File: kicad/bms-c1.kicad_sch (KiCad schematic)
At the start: 33 parts, among them J1 MicroFit 2x12, J2 B4B-PH-SM4, J3 USB_B_Micro, J4 B3B-PH-SM4, J5 B2B-PH-SM4, J6 B4B-PH-SM4, P1 CONN_01X01, P2 CONN_01X01, P3 CONN_01X01, P4 CONN_01X01, P5 CONN_01X01

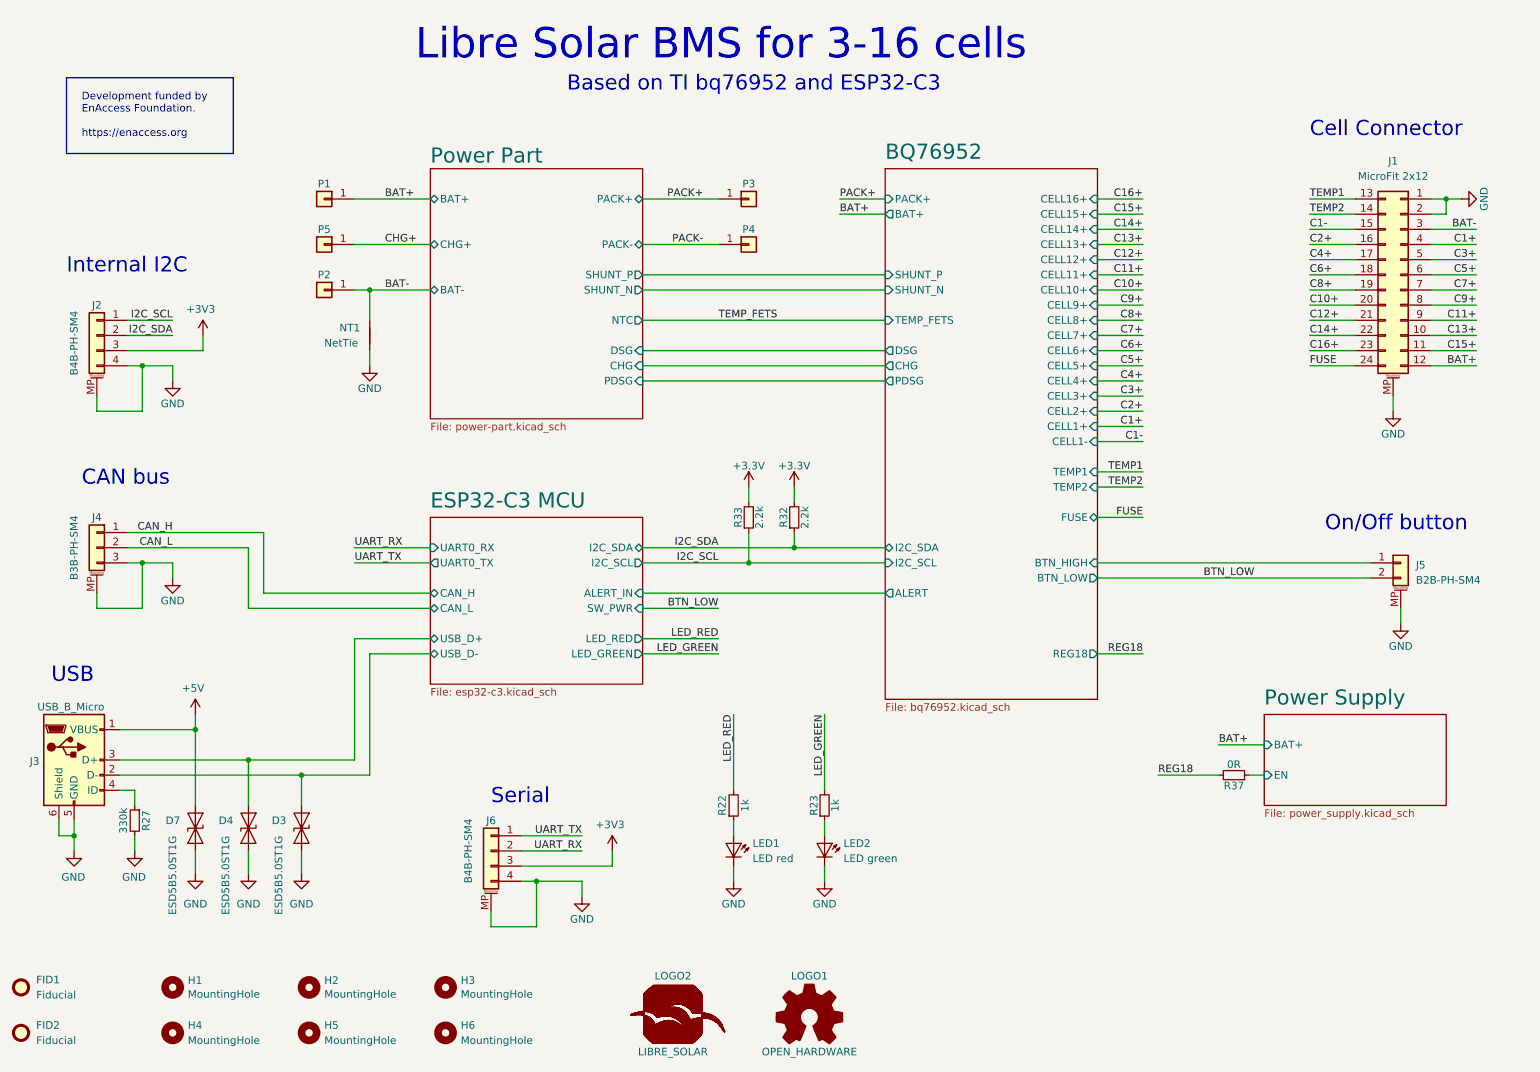
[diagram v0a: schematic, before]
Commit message: v0.4.0: Multiple improvements for new board revision
- Use LMR38010 for internal power supply (max. 80V instead of 60V)
- Change USB connector from Micro-A to C and remove 5V power supply
  which was not working anyway. The board cannot be powered by USB
  only.
- Add TS2 (connected to DFETOFF) to measure shunt temperature
- Add RS-485 transceiver (sharing the connector with CAN)
- Switch I2C pins of ESP32-C3 to GPIO8/9. This allows to re-use the
  I2C pull-ups for strapping configuration and frees two pins for the
  RS-485 transceiver RE and DE pins. Also we may get rid of the I2C
  glitches during start-up.
- Use 80V instead of 100V power MOSFETs to reduce Rds(on).
- Reduce DSG gate resistor R57 to 47R to increase switch-off speed.
- Adjust some resistors to reduce number of different parts
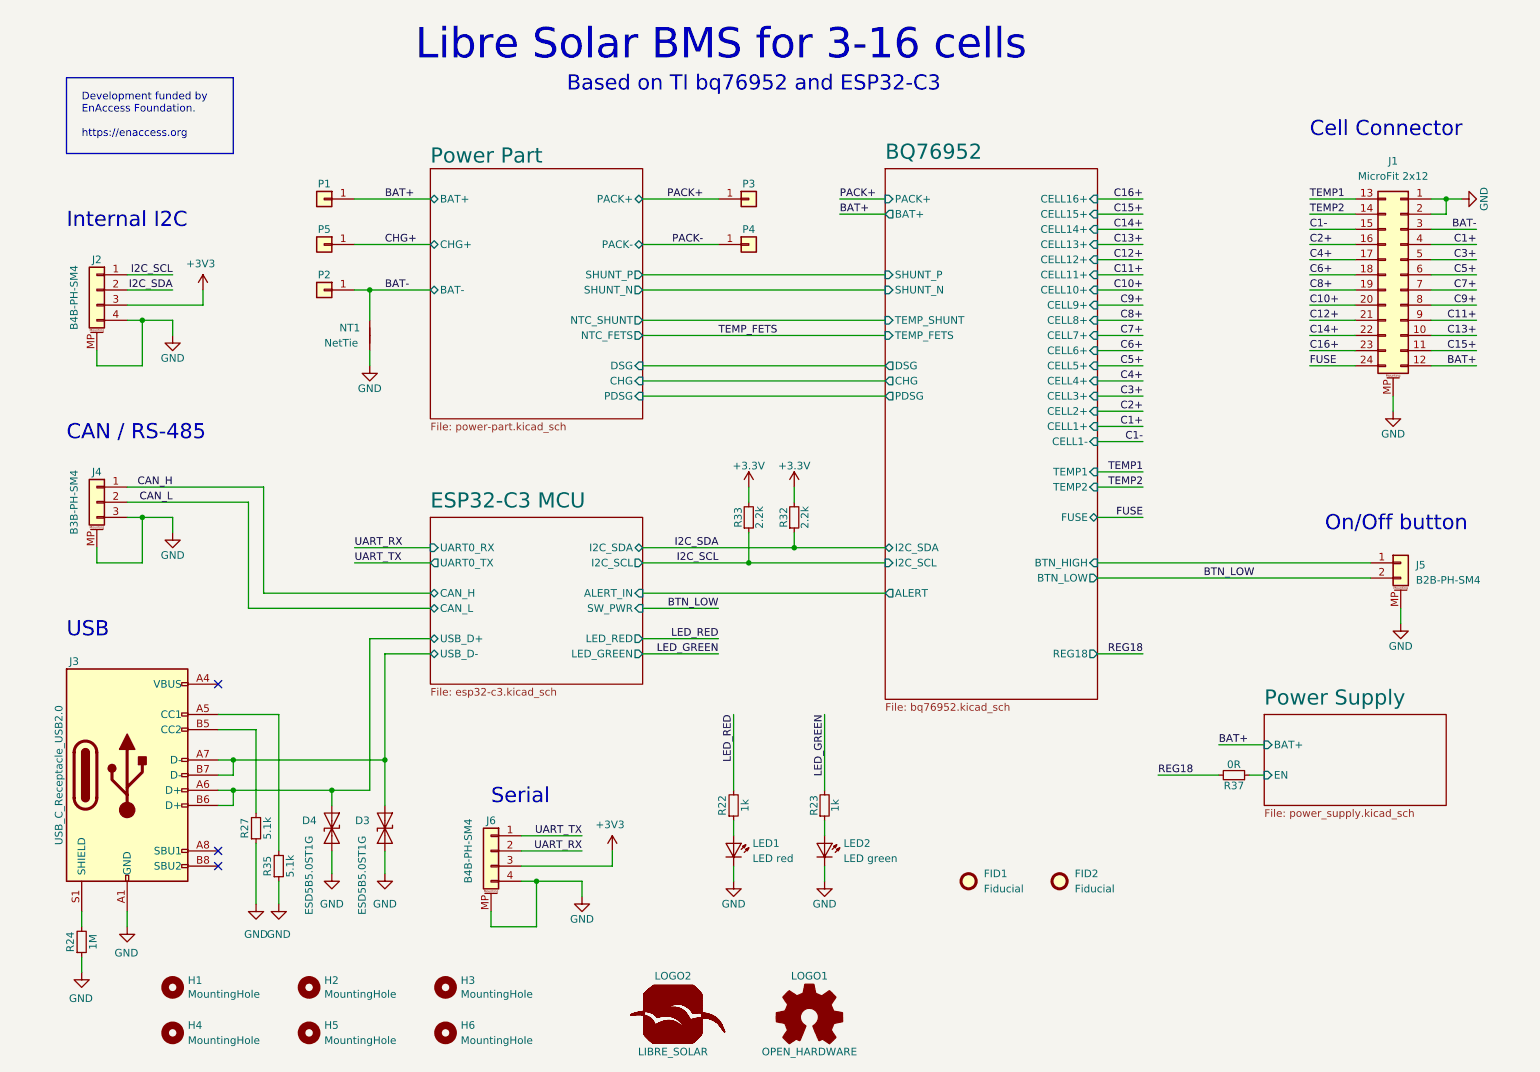
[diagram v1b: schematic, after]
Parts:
- removed D7: ESD5B5.0ST1G, LibreSolar:D_SOD-523, symbol Diode:SZESD9B5.0ST5G
- removed J3: USB_B_Micro, LibreSolar:USB_Micro-B_10103594-0001LF, symbol Connector:USB_B_Micro
- added J3: USB_C_Receptacle_USB2.0, Connector_USB:USB_C_Receptacle_GCT_USB4105-xx-A_16P_TopMnt_Horizontal, symbol Connector:USB_C_Receptacle_USB2.0
- added R24: 1M, LibreSolar:R_0603_1608, symbol LibreSolar:R
- added R35: 5.1k, LibreSolar:R_0603_1608, symbol LibreSolar:R
- D3, D4: LCSC (none) -> C93623
- J1: Manufacturer Molex -> Würth; PartNumber 43045-1810 -> 662024231722; Remarks Alternative: Würth 662024231722, mating connector: 66202411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 -> Mating connector: 662024113322
- J2, J6: LCSC (none) -> C160354
- J4: LCSC (none) -> C160353
- J5: LCSC (none) -> C160352
- LED1: LCSC (none) -> C94869; Manufacturer any -> Lite-On; PartNumber (none) -> LTST-C190KRKT
- LED2: LCSC (none) -> C125094; Manufacturer any -> Lite-On; PartNumber (none) -> LTST-C190KGKT
- P1, P2, P3, P4: LCSC (none) -> C3217898; Manufacturer Würth -> Erni; PartNumber LF990005 -> 225852-E; Remarks Alternative: Erni 225852 -> Alternative: Würth LF990005
- R22, R23: Manufacturer any -> Yageo; PartNumber (none) -> RC0603FR-071KL
- R27: value 330k -> 5.1k; Manufacturer any -> Yageo; PartNumber (none) -> RC0603FR-075K1L
- R32, R33: Manufacturer any -> Yageo; PartNumber (none) -> RC0603FR-072K2L
- R37: Manufacturer any -> Yageo; PartNumber (none) -> RC0603FR-070RL
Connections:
- net ESP32-C3 MCU/USB_D+: now also J3.A6 (D+), J3.B6 (D+)
- net ESP32-C3 MCU/USB_D-: now also J3.A7 (D-), J3.B7 (D-)
- net GND: now also R27.1, J3.A1 (GND), J3.A12 (GND), J3.B1 (GND), J3.B12 (GND), R24.1, R35.1; no longer R27.2
- new net: J3.S1 (SHIELD), R24.2
- new net: J3.B5 (CC2), R27.2
- new net: J3.A5 (CC1), R35.2
- new net: J3.A4 (VBUS), J3.A9 (VBUS), J3.B4 (VBUS), J3.B9 (VBUS)
- no-connect marks 0 -> 3
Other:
- sheet BQ76952 ports: added TEMP_SHUNT; removed none
- sheet Power Part ports: added NTC_FETS, NTC_SHUNT; removed NTC
- note added: "CAN / RS-485"
- note removed: "CAN bus"
- moved on the sheet: D3, D4, FID1, FID2, J2, J4

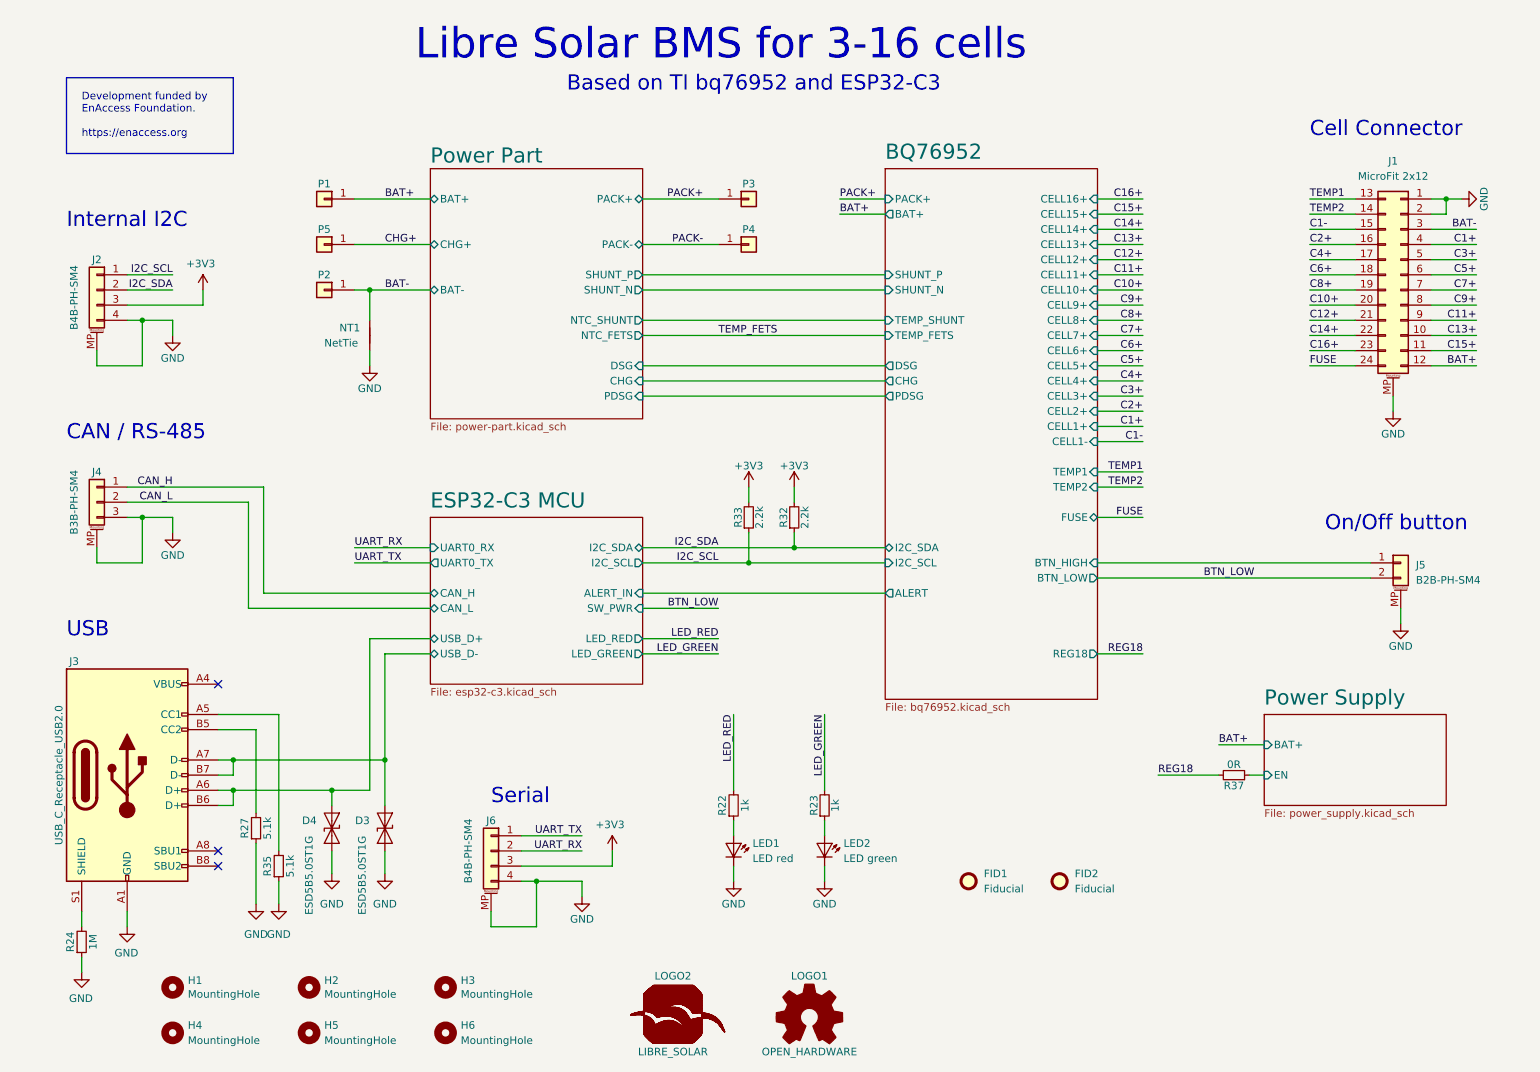
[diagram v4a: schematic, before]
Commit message: Create cost-optimized Lite variant of the BMS C1 v0.4.1
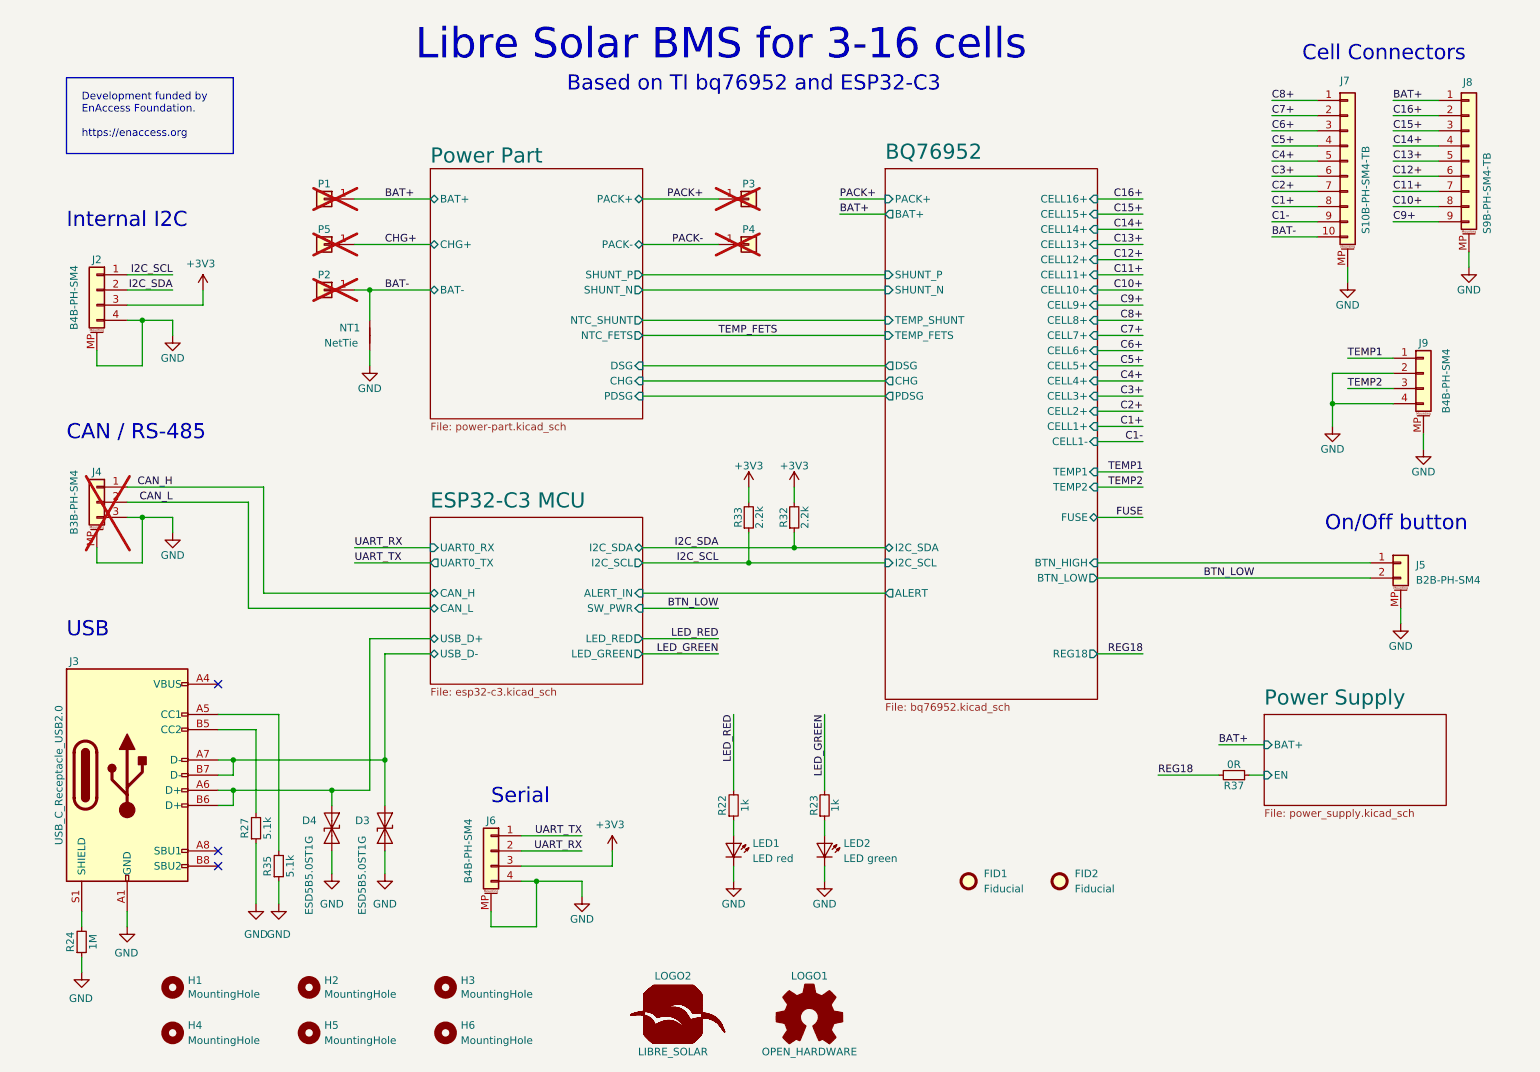
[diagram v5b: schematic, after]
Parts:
- removed J1: MicroFit 2x12, Connector_Molex:Molex_Micro-Fit_3.0_43045-2410_2x12-1MP_P3.00mm_Horizontal, symbol Connector_Generic_MountingPin:Conn_02x12_Top_Bottom_MountingPin
- added J7: S10B-PH-SM4-TB, Connector_JST:JST_PH_S10B-PH-SM4-TB_1x10-1MP_P2.00mm_Horizontal, symbol Connector_Generic_MountingPin:Conn_01x10_MountingPin
- added J8: S9B-PH-SM4-TB, Connector_JST:JST_PH_S9B-PH-SM4-TB_1x09-1MP_P2.00mm_Horizontal, symbol Connector_Generic_MountingPin:Conn_01x09_MountingPin
- added J9: B4B-PH-SM4, Connector_JST:JST_PH_B4B-PH-SM4-TB_1x04-1MP_P2.00mm_Vertical, symbol Connector_Generic_MountingPin:Conn_01x04_MountingPin
- J3: symbol Connector:USB_C_Receptacle_USB2.0 -> Connector:USB_C_Receptacle_USB2.0_16P
- J4, P1, P2, P3, P4, P5: now not fitted
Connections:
- net BAT+: now also J8.1 (Pin_1)
- net BAT-: now also J7.10 (Pin_10)
- net C1+: now also J7.8 (Pin_8)
- net C1-: now also J7.9 (Pin_9)
- net C10+: now also J8.8 (Pin_8)
- net C11+: now also J8.7 (Pin_7)
- net C12+: now also J8.6 (Pin_6)
- net C13+: now also J8.5 (Pin_5)
- net C14+: now also J8.4 (Pin_4)
- net C15+: now also J8.3 (Pin_3)
- net C16+: now also J8.2 (Pin_2)
- net C2+: now also J7.7 (Pin_7)
- net C3+: now also J7.6 (Pin_6)
- net C4+: now also J7.5 (Pin_5)
- net C5+: now also J7.4 (Pin_4)
- net C6+: now also J7.3 (Pin_3)
- net C7+: now also J7.2 (Pin_2)
- net C8+: now also J7.1 (Pin_1)
- net C9+: now also J8.9 (Pin_9)
- net GND: now also J7.MP (MountPin), J8.MP (MountPin), J9.2 (Pin_2), J9.4 (Pin_4), J9.MP (MountPin)
- net TEMP1: now also J9.1 (Pin_1)
- net TEMP2: now also J9.3 (Pin_3)
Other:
- note added: "Cell Connectors"
- note removed: "Cell Connector"
- title: Libre Solar BMS C1 -> Libre Solar BMS C1 lite
